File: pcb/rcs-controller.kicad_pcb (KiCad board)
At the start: 2 copper layers, 64 x 73 mm, 92 parts, among them J1 00222-32051, J10 0022-232021, J2 0022-232021, J3 0022-232041, J4 Screw_Terminal_4_P3.50mm, J8 00222-32051, Q1 SI7465DP-T1-E3, Q2 SI7465DP-T1-E3, Q3 SI7465DP-T1-E3, Q4 PMV45EN2, Q5 PMV45EN2, U1 LSM6DSOX, U2 MP26123DR-LF-Z, U3 TPS63070, U4 ESP32-WROOM-32UE

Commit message: Revision 6/2
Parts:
- removed TP1, TP2, TP3, TP32: Test-Point, psas-footprints:TP-through-hole-1X01
- added C21: 1p, Capacitor_SMD:C_0603_1608Metric, F.Cu at (83.9, 107.3)
- added C22: 1p, Capacitor_SMD:C_0603_1608Metric, F.Cu at (94.9, 91.7)
- added J1: 00222-32051, Connector_Molex:Molex_KK-254_AE-6410-06A_1x06_P2.54mm_Vertical, F.Cu at (132.1, 81.6)
- added R28: 5k, Resistor_SMD:R_0603_1608Metric, F.Cu at (91.3, 103.2)
- added R29: 5k, Resistor_SMD:R_0603_1608Metric, F.Cu at (91.1, 95.3)
- added R30: 10k, Resistor_SMD:R_0603_1608Metric, F.Cu at (94.9, 88.7)
- added REF**: SW_PUSH_6mm, Button_Switch_THT:SW_PUSH_6mm, F.Cu at (83.5, 93.7)
- added REF**: USB_C_Receptacle_Palconn_UTC16-G, Connector_USB:USB_C_Receptacle_Palconn_UTC16-G, F.Cu at (86.8, 100.5)
- U4: value ESP32-WROOM-32UE -> ESP32-S3-WROOM-1; footprint RF_Module:ESP32-WROOM-32UE -> RF_Module:ESP32-S3-WROOM-1
- moved C19 55.1 mm to (93.5, 81.2), turned to 0 degrees
- moved D5 53.1 mm to (86.9, 139.4)
- moved R16 53.1 mm to (86.9, 136.4)
- moved C20 50.5 mm to (94.2, 83.5), turned to 90 degrees
- moved TP6 50.4 mm to (87.0, 133.8), turned to 180 degrees
- moved U1 50.2 mm to (91.9, 83.8), turned to 90 degrees
- moved TP7 47.2 mm to (116.5, 147.7)
- moved C14 44.0 mm to (90.1, 132.9), turned to 90 degrees
- moved R9 41.5 mm to (90.3, 129.7), turned to 0 degrees
- moved TP30 40.8 mm to (90.3, 128.1), turned to 180 degrees
- moved C15 40.3 mm to (92.1, 132.9), turned to 90 degrees
- moved L1 40.3 mm to (95.3, 137.8), turned to 180 degrees
- moved R10 36.6 mm to (92.6, 128.8), turned to 90 degrees
- moved LOGO1 35.8 mm to (126.5, 92.5)
- moved R20 35.3 mm to (100.5, 139.1), turned to -90 degrees
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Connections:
- U4 pad 12: unconnected-(U4-IO27-Pad12) -> UMB_~{ON}
- U4 pad 13: unconnected-(U4-IO14-Pad13) -> Net-(U4-USB_D-)
- U4 pad 14: unconnected-(U4-IO12-Pad14) -> Net-(U4-USB_D+)
- U4 pad 15: GND -> Net-(U1-CS)
- U4 pad 17: unconnected-(U4-NC-Pad17) -> BATT_READ
- U4 pad 24: Net-(U1-CS) -> unconnected-(U4-IO47-Pad24)
- U4 pad 25: Net-(U1-SCL) -> unconnected-(U4-IO48-Pad25)
- U4 pad 26: Net-(U1-INT1) -> unconnected-(U4-IO45-Pad26)
- U4 pad 36: UMB_~{ON} -> Net-(J6-Pin_1)
- U4 pad 37: BATT_READ -> Net-(J6-Pin_2)
- U4 pad 38: GND -> Net-(U1-SCL)
- U4 pad 39: GND -> unconnected-(U4-IO1-Pad39)
- U4 pad 4: unconnected-(U4-SENSOR_VP-Pad4) -> Net-(U1-INT1)
- U4 pad 6: Net-(Q4-G) -> unconnected-(U4-IO6-Pad6)
- U4 pad 7: Net-(Q5-G) -> unconnected-(U4-IO7-Pad7)
- U4 pad 8: unconnected-(U4-IO32-Pad8) -> Net-(Q4-G)
- U4 pad 9: unconnected-(U4-IO33-Pad9) -> Net-(Q5-G)
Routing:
- net Net-(U1-SCL): track 26.0 -> 69.7 mm, vias 0 -> 2
- net BATT_READ: track 13.6 -> 45.2 mm
- net +BATT: track 98.6 -> 73.3 mm
- net Net-(C22-Pad1): track 0.00 -> 24.2 mm, vias 0 -> 1
- net +3.3V: track 139.3 -> 118.5 mm, vias 0 -> 4
- net Net-(J6-Pin_1): track 0.00 -> 19.7 mm
- net VBUS: track 32.0 -> 12.8 mm
- net Net-(J5-SHIELD): track 0.00 -> 18.8 mm
- net Net-(J2-Pin_1): track 91.8 -> 73.9 mm, vias 0 -> 2
- net Net-(U1-INT1): track 19.2 -> 5.75 mm, vias 2 -> 0
- net Net-(U4-USB_D+): track 0.00 -> 12.7 mm
- net Net-(U4-USB_D-): track 0.00 -> 12.1 mm
- net CANL: track 41.9 -> 31.3 mm, vias 0 -> 1
- net Net-(J6-Pin_2): track 0.00 -> 10.3 mm
- net Net-(Q4-G): track 46.8 -> 55.2 mm
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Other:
- board size 64 x 73 mm -> 64 x 75.3 mm

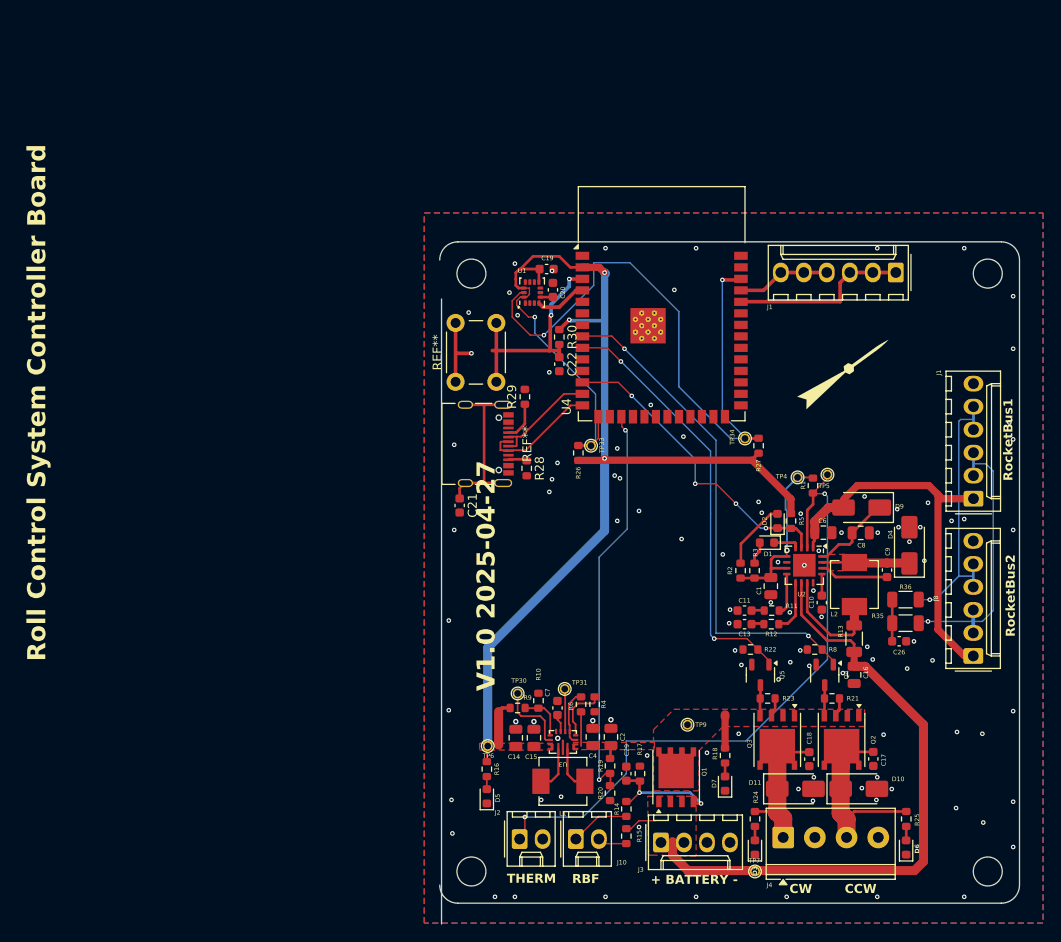
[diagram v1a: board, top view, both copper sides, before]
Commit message: Design review; fix schematic issues and some polish, some board to schematic patching, fix footprint issues.
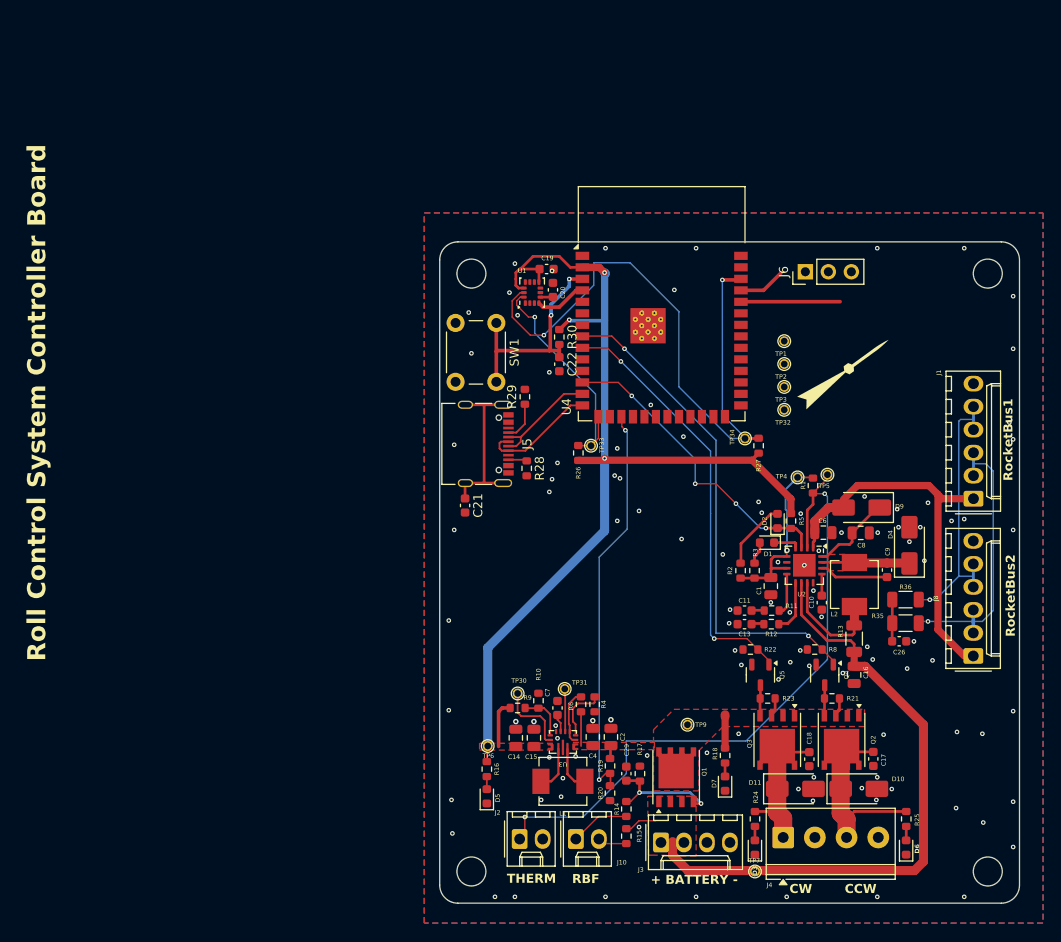
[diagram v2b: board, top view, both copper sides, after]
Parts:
- removed the J1 at (132.1, 81.6)
- removed the REF** at (83.5, 93.7)
- removed the REF** at (86.8, 100.5)
- added J5: USB_C_Receptacle_USB2.0_14P, Connector_USB:USB_C_Receptacle_Palconn_UTC16-G, F.Cu at (86.8, 100.5)
- added J6: Conn_01x03, Connector_PinHeader_2.54mm:PinHeader_1x03_P2.54mm_Vertical, F.Cu at (122.1, 81.5)
- added SW1: SW_Push, Button_Switch_THT:SW_PUSH_6mm, F.Cu at (88.0, 87.2)
- added TP1: Test-Point, psas-footprints:TP-through-hole-1X01, F.Cu at (119.7, 89.2)
- added TP2: Test-Point, psas-footprints:TP-through-hole-1X01, F.Cu at (119.7, 91.7)
- added TP3: Test-Point, psas-footprints:TP-through-hole-1X01, F.Cu at (119.7, 94.2)
- added TP32: Test-Point, psas-footprints:TP-through-hole-1X01, F.Cu at (119.7, 96.7)
- C22: value 1p -> 100p
- R26, R27: value 10k -> 4.7k
- moved C21 0.60 mm to (84.5, 107.3)
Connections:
- net Net-(U1-INT1) renamed /Microcontroller/INT1
- net Net-(U1-SCL) renamed /Microcontroller/SCL
- C22 pad 1: Net-(C22-Pad1) -> Net-(U4-EN)
- R26 pad 2: Net-(U1-CS) -> /Microcontroller/SDA
- R30 pad 2: Net-(C22-Pad1) -> Net-(U4-EN)
- TP33 pad 1: Net-(U1-CS) -> /Microcontroller/SDA
- U1 pad 12: Net-(U1-CS) -> +3.3V
- U1 pad 14: Net-(U1-CS) -> /Microcontroller/SDA
- U4 pad 15: Net-(U1-CS) -> /Microcontroller/SDA
- U4 pad 3: +3.3V -> Net-(U4-EN)
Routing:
- net Net-(U1-CS): track 28.1 -> 0.00 mm, vias 1 -> 0
- net /Microcontroller/SDA: track 0.00 -> 26.1 mm, vias 0 -> 1
- net Net-(U4-EN): track 0.00 -> 25.3 mm, vias 0 -> 2
- net Net-(C22-Pad1): track 24.2 -> 0.00 mm, vias 1 -> 0
- net Net-(J6-Pin_1): track 19.7 -> 11.0 mm
- net GND: track 8.48 -> 0.28 mm, vias 103 -> 107
- net Net-(J6-Pin_2): track 10.3 -> 5.26 mm
- net +3.3V: track 118.5 -> 117.2 mm, vias 4 -> 3
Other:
- board size 64 x 75.3 mm -> 64 x 73 mm
- board text removed: "V${REVISION} ${ISSUE_DATE}"

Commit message: Rev date 6.15
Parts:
- moved C21 56.8 mm to (140.4, 97.2), turned to 180 degrees
- moved J5 53.2 mm to (139.9, 103.6), turned to 90 degrees
- moved R29 45.9 mm to (135.6, 106.5), turned to -90 degrees
- moved J2 44.2 mm to (109.9, 104.4), turned to -90 degrees
- moved R28 44.2 mm to (135.4, 100.9), turned to 90 degrees
- moved C19 41.1 mm to (112.9, 117.4)
- moved C20 40.0 mm to (112.9, 118.9), turned to 0 degrees
- moved U1 38.9 mm to (109.9, 118.3)
- moved TP1 37.8 mm to (136.2, 123.2)
- moved J10 36.1 mm to (109.9, 110.5), turned to -90 degrees
- moved TP32 32.8 mm to (136.2, 125.1)
- moved SW1 29.7 mm to (117.5, 84.5), turned to 180 degrees
- moved TP6 28.2 mm to (112.3, 121.3), turned to 90 degrees
- moved D5 28.0 mm to (110.0, 123.5), turned to 180 degrees
- moved R9 27.5 mm to (117.5, 125.8), turned to 180 degrees
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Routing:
- net /Microcontroller/SCL: track 69.7 -> 4.00 mm, vias 2 -> 0
- net +BATT: track 73.3 -> 10.9 mm
- net Net-(J2-Pin_1): track 73.9 -> 20.0 mm, vias 2 -> 0
- net Net-(Q4-G): track 55.2 -> 1.67 mm, vias 2 -> 0
- net Net-(Q5-G): track 47.2 -> 1.67 mm, vias 2 -> 0
- net BATT_READ: track 45.2 -> 0.00 mm, vias 2 -> 0
- net VBUS: track 12.8 -> 45.0 mm, vias 0 -> 3
- net UMB_~{ON}: track 34.2 -> 5.70 mm, vias 4 -> 0
- net +3.3V: track 117.2 -> 88.9 mm, vias 3 -> 0
- net /Microcontroller/SDA: track 26.1 -> 5.06 mm, vias 1 -> 0
- net Net-(U4-USB_D-): track 12.3 -> 30.5 mm
- net Net-(U4-USB_D+): track 13.0 -> 28.3 mm
- net /Power/VUMB: track 43.4 -> 31.3 mm
- net /Power/VREF33: track 20.2 -> 10.6 mm, vias 1 -> 0
- net Net-(D10-K): track 21.4 -> 11.9 mm
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- removed copper zone on F.Cu, net +3.3V
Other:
- board size 64 x 73 mm -> 43.1 x 73 mm
- board text added: "V${REVISION} ${ISSUE_DATE}"

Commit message: rev date 6.16.2025
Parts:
- moved C19 27.4 mm to (116.3, 90.2)
- moved C20 27.4 mm to (116.3, 91.7)
- moved R26 27.4 mm to (109.4, 94.8)
- moved R27 27.4 mm to (109.4, 90.0)
- moved TP33 27.4 mm to (110.2, 93.2)
- moved TP34 27.4 mm to (110.2, 91.6)
- moved U1 27.4 mm to (113.3, 91.1)
- moved R19 26.4 mm to (120.5, 112.5), turned to 90 degrees
- moved R20 26.4 mm to (119.0, 112.5), turned to -90 degrees
- moved C14 26.0 mm to (128.6, 102.2)
- moved C15 26.0 mm to (128.6, 104.2)
- moved TP31 25.4 mm to (134.2, 111.6)
- moved J10 24.9 mm to (104.8, 134.9)
- moved C2 24.6 mm to (128.7, 115.3)
- moved C4 24.6 mm to (128.7, 113.3)
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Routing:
- net Net-(Q4-G): track 1.67 -> 44.3 mm, vias 0 -> 2
- net Net-(Q5-G): track 1.67 -> 40.9 mm, vias 0 -> 2
- net UMB_~{ON}: track 5.70 -> 40.3 mm, vias 0 -> 2
- net /Microcontroller/SCL: track 4.00 -> 35.3 mm, vias 0 -> 1
- net /Power/VUMB: track 31.3 -> 55.3 mm, vias 0 -> 1
- net +BATT: track 10.9 -> 32.8 mm, vias 0 -> 1
- net BATT_READ: track 0.00 -> 21.0 mm, vias 0 -> 2
- net /Power/ARM-IN: track 0.00 -> 18.4 mm, vias 0 -> 1
- net /Microcontroller/INT1: track 0.00 -> 15.2 mm, vias 0 -> 2
- net /Microcontroller/SDA: track 5.06 -> 19.5 mm, vias 0 -> 1
- net +3.3V: track 88.9 -> 98.4 mm
- net /Power/VREF33: track 10.6 -> 18.4 mm, vias 0 -> 1
- net /Power/ARM-OUT: track 0.00 -> 6.84 mm
- net Net-(Q2-G): track 4.90 -> 10.4 mm, vias 0 -> 2
- net Net-(U3-FB2): track 5.52 -> 1.33 mm
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- added copper zone on F.Cu, net (none)
- removed copper zone on F.Cu, net Net-(D4-K)
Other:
- board size 43.1 x 73 mm -> 45.6 x 73 mm

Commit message: Cleaner board
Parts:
- moved REF** 18.4 mm to (103.6, 81.7)
- moved REF** 18.4 mm to (103.6, 147.7)
- moved D4 10.8 mm to (115.6, 125.1), turned to -90 degrees
- moved C9 9.27 mm to (113.0, 123.3)
- moved C26 6.67 mm to (135.5, 115.1)
- moved C16 5.89 mm to (110.2, 128.2)
- moved R13 3.66 mm to (110.7, 130.4)
- moved C1 3.62 mm to (105.8, 125.6)
- moved C8 3.62 mm to (115.7, 119.7)
- moved R2 3.62 mm to (102.5, 123.9)
- moved R5 3.62 mm to (106.1, 118.5)
- moved C6 3.62 mm to (112.3, 119.7)
- moved R1 3.62 mm to (109.5, 117.2)
- moved TP4 3.62 mm to (109.5, 114.9)
- moved C13 3.62 mm to (104.0, 130.4)
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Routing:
- net +3.3V: track 98.4 -> 76.5 mm
- net +BATT: track 32.8 -> 11.9 mm, vias 1 -> 0
- net CANL: track 33.0 -> 21.2 mm
- net /Power/VREF33: track 18.4 -> 7.28 mm
- net Net-(J2-Pin_1): track 16.8 -> 6.03 mm
- net UMB_~{ON}: track 40.3 -> 29.6 mm
- net Net-(D11-K): track 11.3 -> 4.05 mm
- net Net-(D10-K): track 11.9 -> 4.85 mm
- net /Power/ARM-OUT: track 6.84 -> 0.00 mm
- net Net-(U2-CSP): track 10.2 -> 17.0 mm
- net Net-(D2-A): track 6.26 -> 0.00 mm
- net Net-(U2-BST): track 7.76 -> 1.75 mm
- net VBUS: track 42.3 -> 36.8 mm, vias 0 -> 2
- net /Power/VUMB: track 55.3 -> 57.8 mm, vias 1 -> 0
- net Net-(Q2-G): track 10.4 -> 8.09 mm
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- added copper zone on F.Cu, net Net-(D10-K)
- added copper zone on F.Cu, net Net-(D11-K)
- removed copper zone on F.Cu, net (none)

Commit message: Rev. 6.17
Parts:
- moved TP3 59.6 mm to (104.7, 141.6)
- moved TP5 1.21 mm to (111.3, 114.9)
- moved R21 1.20 mm to (134.7, 128.5)
- moved R23 1.10 mm to (127.3, 128.5)
- moved LOGO1 1.03 mm to (105.8, 100.1)
- moved TP7 0.71 mm to (108.0, 141.6)
- moved J2 0.61 mm to (105.9, 108.2)
- moved TP30 0.50 mm to (128.7, 106.8)
- moved C21 0.40 mm to (140.4, 97.6)
- moved J10 0.30 mm to (105.6, 134.9)
- moved R28 0.20 mm to (136.6, 100.3)
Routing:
- net CANL: track 21.2 -> 58.5 mm
- net +3.3V: track 76.5 -> 102.9 mm
- net UMB_~{ON}: track 29.6 -> 41.3 mm
- net /Power/VREF33: track 7.28 -> 18.6 mm, vias 1 -> 2
- net Net-(J2-Pin_1): track 6.03 -> 16.5 mm
- net +BATT: track 11.9 -> 20.8 mm
- net /Power/ARM-OUT: track 0.00 -> 6.43 mm, vias 0 -> 1
- net Net-(D2-A): track 0.00 -> 6.26 mm
- net Net-(Q3-G): track 9.20 -> 7.41 mm
- net Net-(U3-FB2): track 1.33 -> 2.05 mm
- net Net-(U3-FB): track 4.89 -> 5.53 mm
- net Net-(U2-CSP): track 17.0 -> 16.3 mm
- net Net-(D1-K): track 2.60 -> 3.16 mm
- net VBUS: track 36.8 -> 36.2 mm
- net Net-(Q2-G): track 8.09 -> 7.58 mm

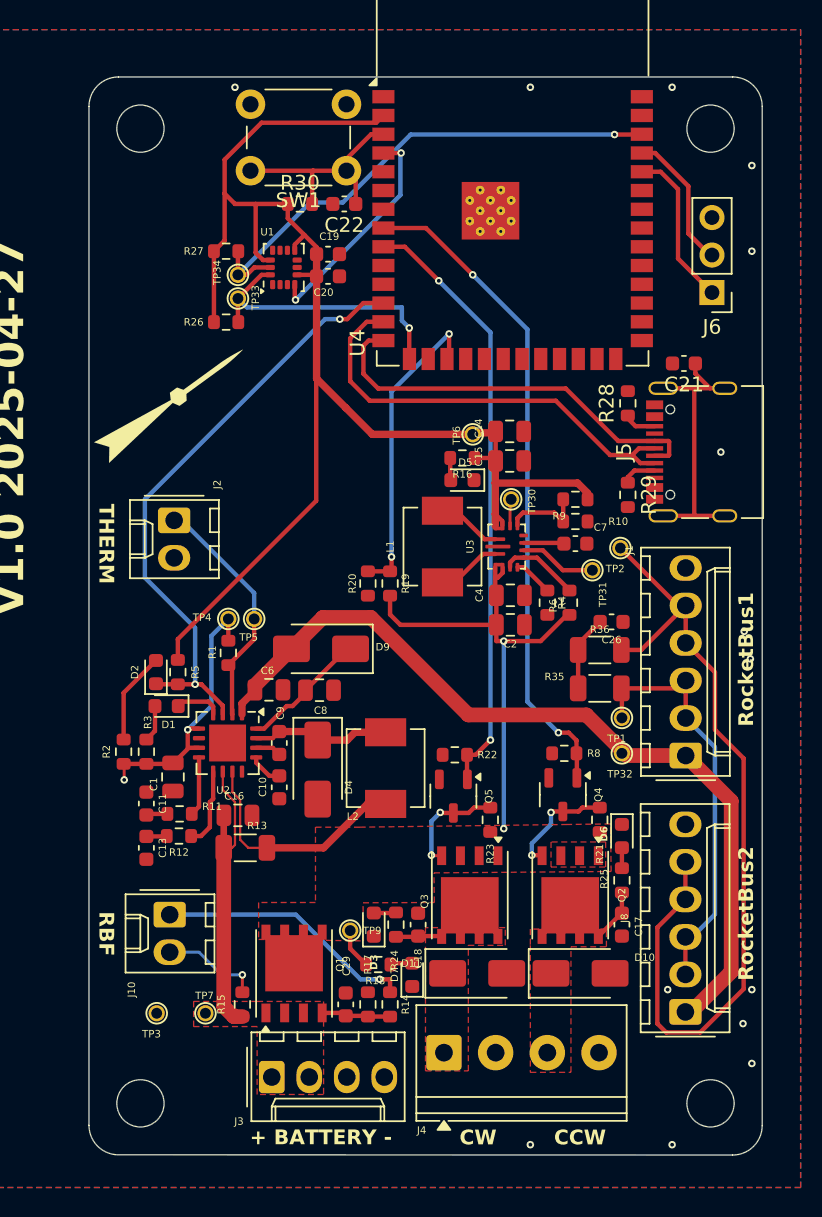
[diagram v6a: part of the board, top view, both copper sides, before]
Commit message: Board design review; fix DRC errors. Back to Jacob for polishing.
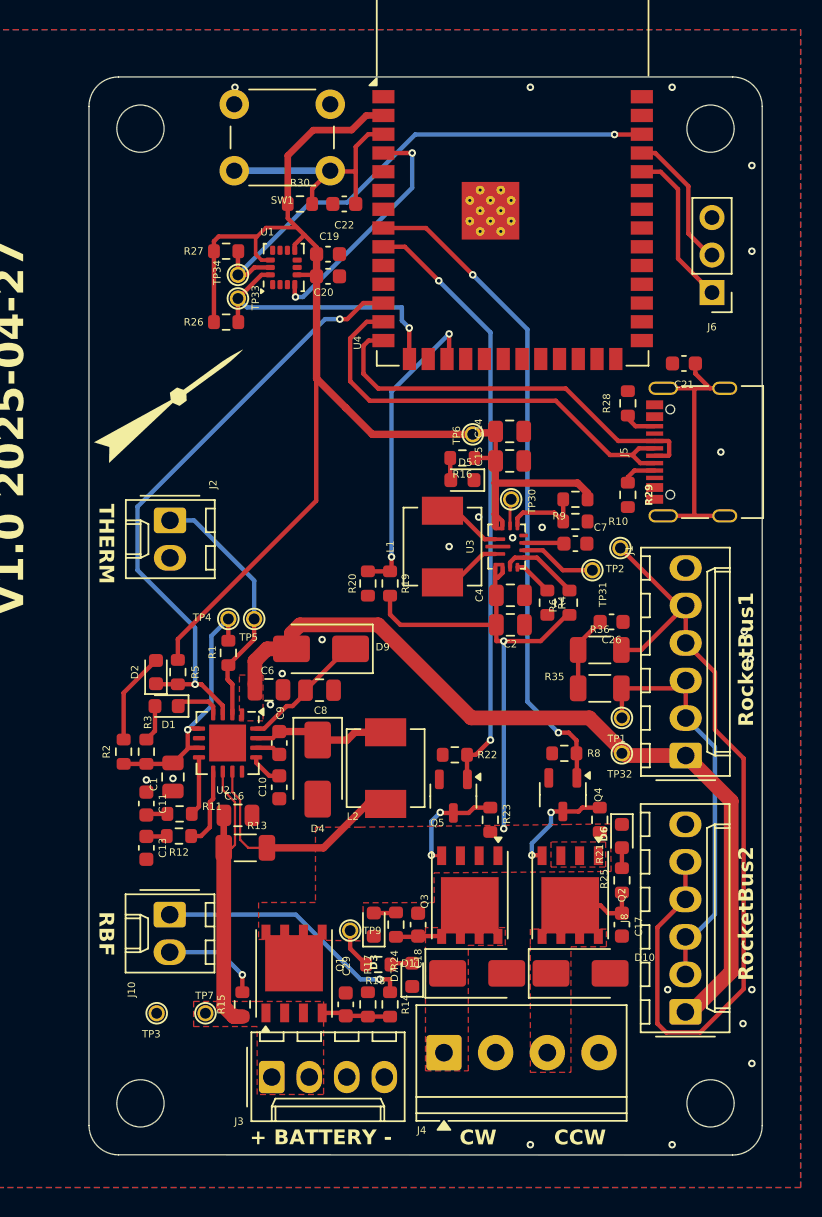
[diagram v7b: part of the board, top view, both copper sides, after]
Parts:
- moved SW1 1.10 mm to (116.5, 84.5)
- moved J2 0.28 mm to (105.6, 108.2)
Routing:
- net +3.3V: track 102.9 -> 95.7 mm
- net Net-(U4-EN): track 15.3 -> 17.1 mm
- net Net-(D10-K): track 4.85 -> 6.33 mm
- net Net-(J2-Pin_1): track 16.5 -> 17.6 mm
- net /Power/VREF33: track 18.6 -> 17.6 mm, vias 2 -> 1
- net /Microcontroller/INT1: track 15.2 -> 16.1 mm
- net /Power/VUMB: track 57.4 -> 56.6 mm
- net GND: vias 14 -> 23
- added copper zone on F.Cu, net /Power/VUMB
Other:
- outline, holes or cut-outs redrawn

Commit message: Silkscreen clean up
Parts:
- moved LOGO1 0.78 mm to (106.5, 100.5)
